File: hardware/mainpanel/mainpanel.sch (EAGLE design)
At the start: 9 parts, among them J1 90136-106, J2 90136-104, J3 90136-104, J4 90136-108, J5 90136-104

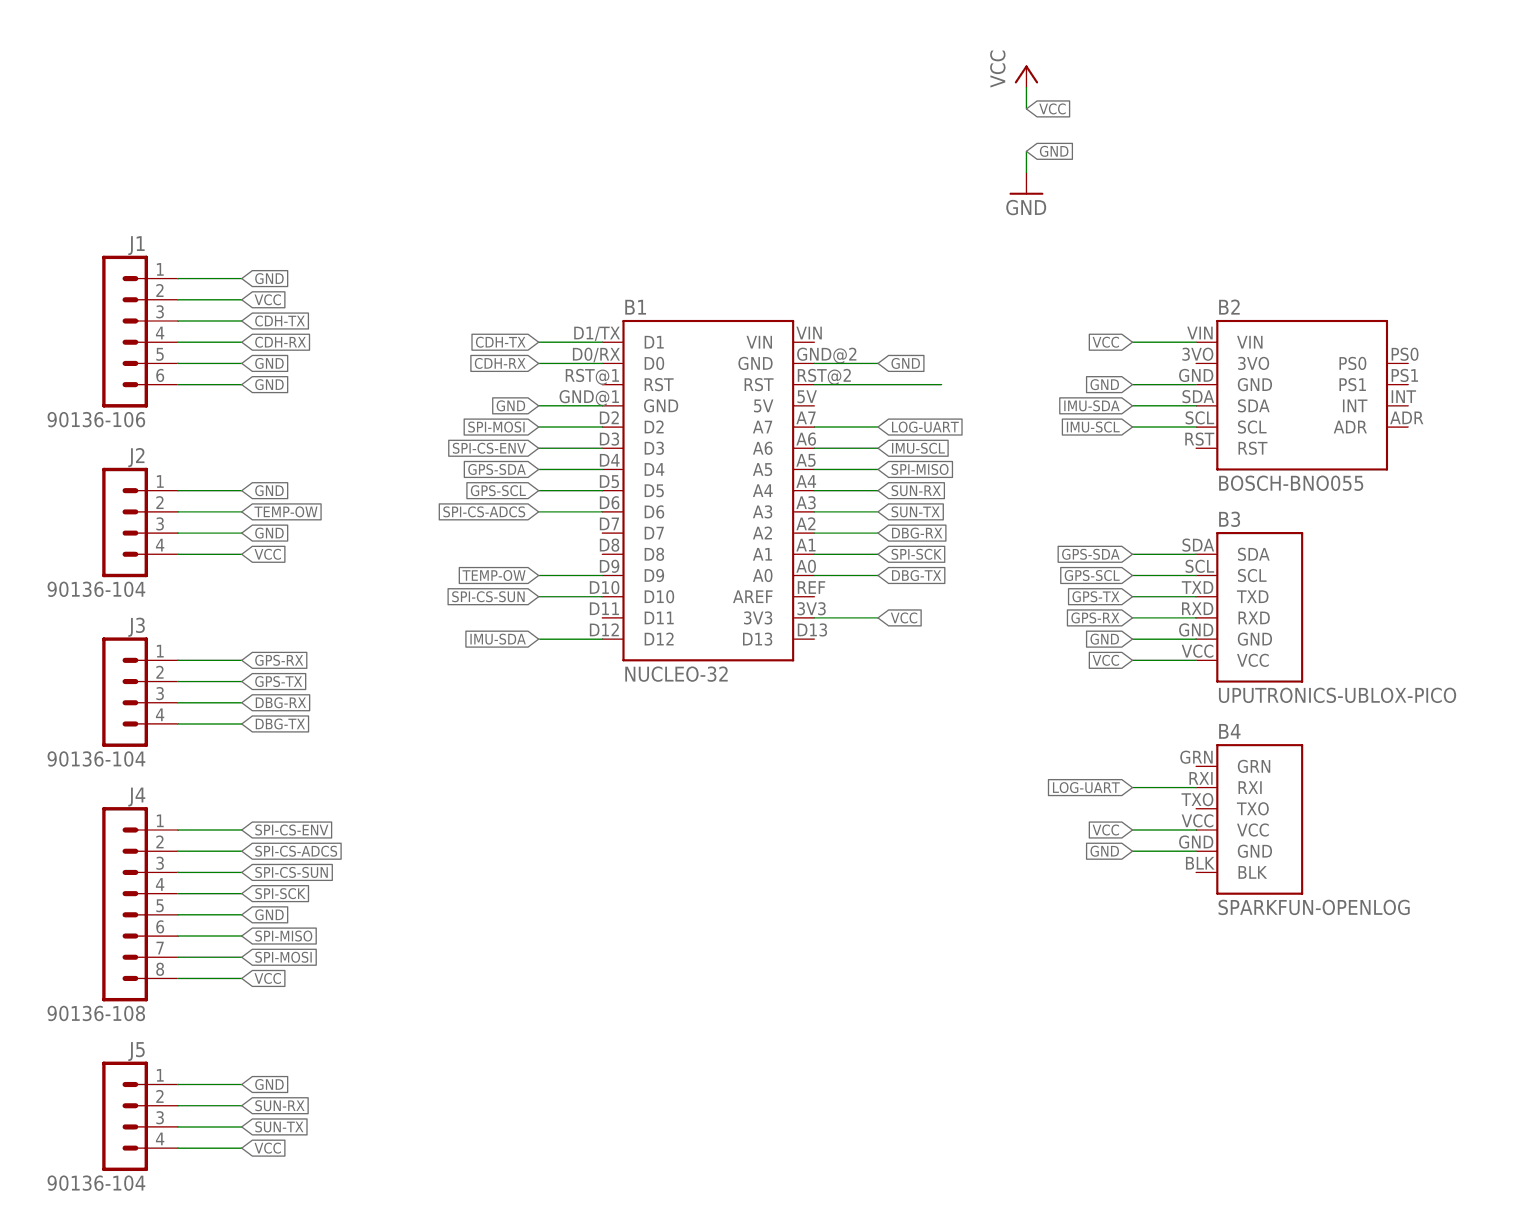
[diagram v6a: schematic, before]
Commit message: Move parts on sch
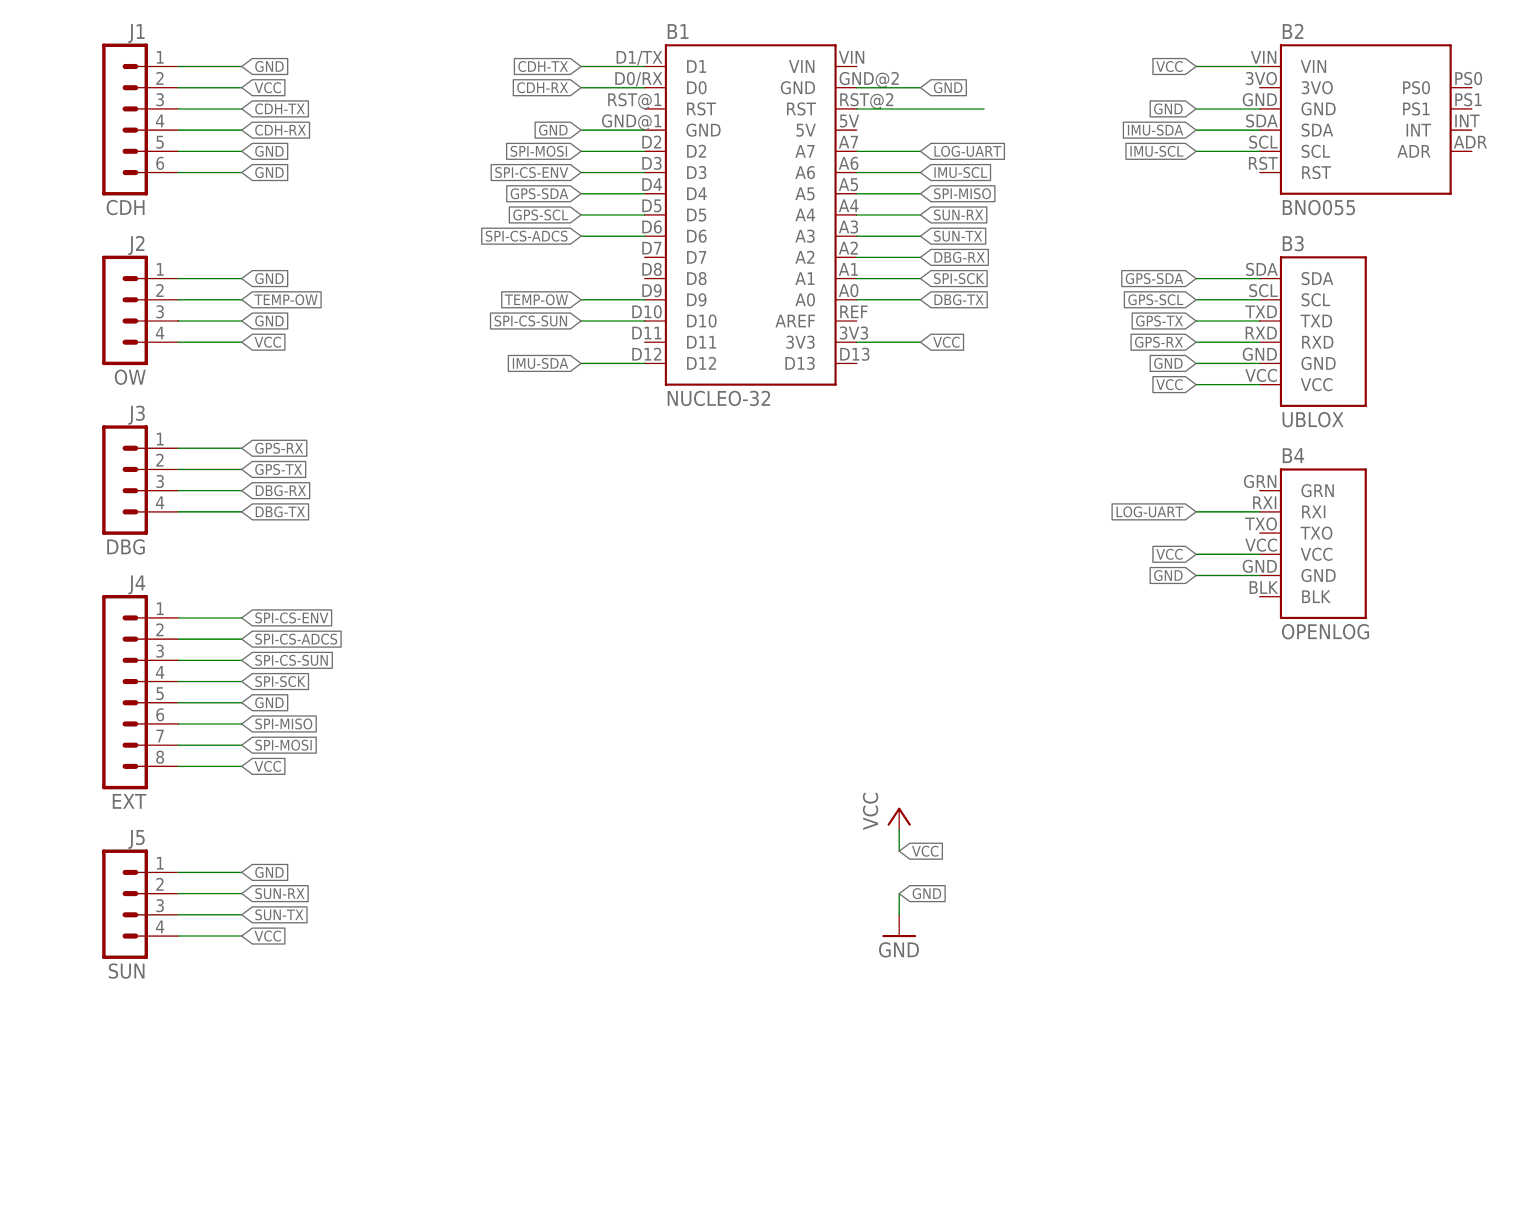
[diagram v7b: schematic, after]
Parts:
- B2: value BOSCH-BNO055 -> BNO055
- B3: value UPUTRONICS-UBLOX-PICO -> UBLOX
- B4: value SPARKFUN-OPENLOG -> OPENLOG
- J1: value 90136-106 -> CDH
- J2: value 90136-104 -> OW
- J3: value 90136-104 -> DBG
- J4: value 90136-108 -> EXT
- J5: value 90136-104 -> SUN
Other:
- moved on the sheet: B1, B2, B3, B4, J1, J2, J3, J4, J5

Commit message: Add DS18B20 sensors
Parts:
- added R1: 4.7k, resistor:R-EU_M2012
- added U1, U2: DS18B20, Frcy:DS18B20
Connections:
- net GND: now also J2.2, U1.GND, U2.GND; no longer J2.3
- net TEMP-OW: now also J2.3, R1.1, U1.DQ, U2.DQ; no longer J2.2
- net VCC: now also R1.2, U1.VDD, U2.VDD
